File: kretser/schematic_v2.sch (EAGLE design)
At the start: 16 parts, among them IC1 ATMEGA168-20PU, U2 LM2940CT-5.0/NOPB

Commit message: updated krets, updated programs
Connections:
- removed net V_OUT: C2.1, C3.1, C5.1, D2.C, IC1.AVCC, IC1.VCC@1, R2.2, R4.2, SPI.2, U2.OUT
- new net N$2: C3.1, IC1.VCC@1
- new net N$5: C5.1, IC1.AVCC
- new net VCC: C2.1, D2.C, R2.2, R4.2, SPI.2, U2.OUT
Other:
- note added: "LDO_MODULE"
- moved on the sheet: C1, C2, R4, U2

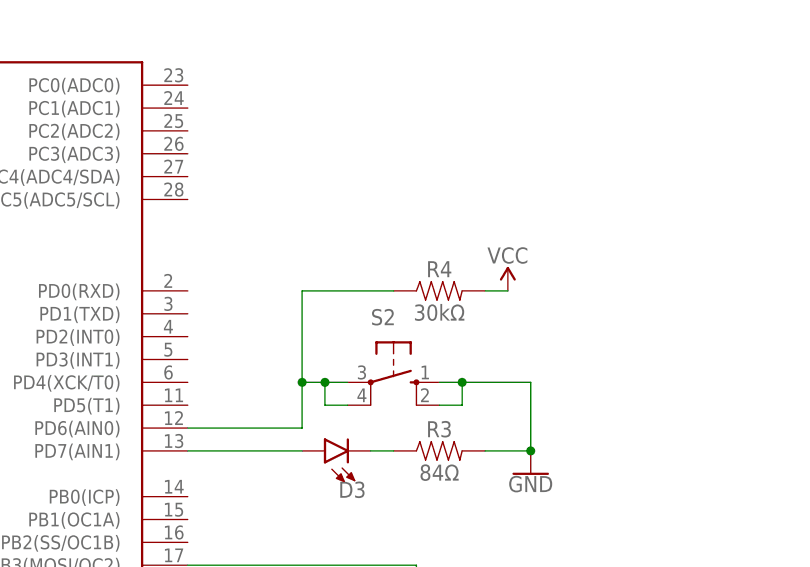
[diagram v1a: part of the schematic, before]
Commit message: updated button codes, updated krets
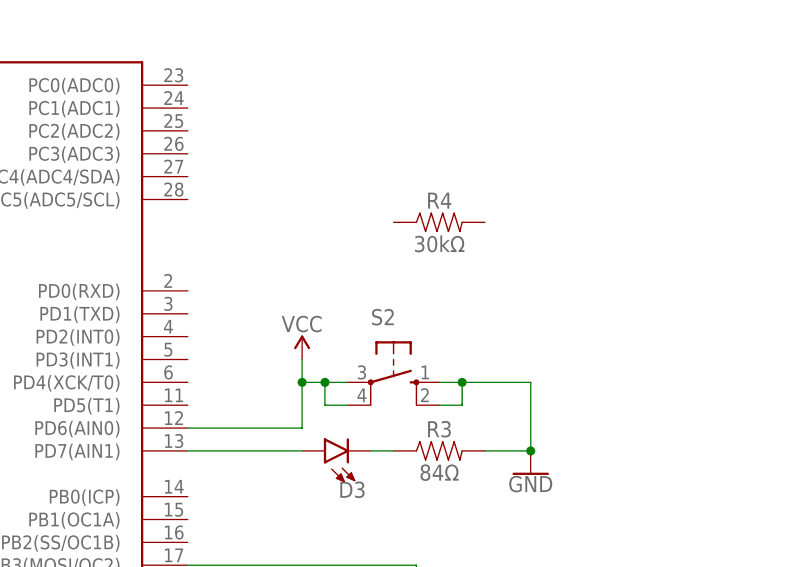
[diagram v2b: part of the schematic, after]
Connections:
- removed net N$8: IC1.PD6(AIN0), R4.1, S2.P, S2.P1
- net VCC: now also IC1.PD6(AIN0), S2.P, S2.P1; no longer R4.2
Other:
- moved on the sheet: R4
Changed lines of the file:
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@@
 <attribute name="VALUE" x="170.815" y="85.09" size="1.778" layer="96"/>
 </instance>
-<instance part="R4" gate="G$1" x="172.72" y="91.44" smashed="yes">
-<attribute name="NAME" x="172.72" y="92.964" size="1.778" layer="95" font="vector" align="bottom-center"/>
-<attribute name="VALUE" x="172.72" y="89.916" size="1.778" layer="96" font="vector" align="top-center"/>
+<instance part="R4" gate="G$1" x="172.72" y="99.06" smashed="yes">
+<attribute name="NAME" x="172.72" y="100.584" size="1.778" layer="95" font="vector" align="bottom-center"/>
+<attribute name="VALUE" x="172.72" y="97.536" size="1.778" layer="96" font="vector" align="top-center"/>
 </instance>
 <instance part="C5" gate="G$1" x="86.36" y="106.68" smashed="yes" rot="R180">
@@
 <attribute name="VALUE" x="73.66" y="139.446" size="1.778" layer="96" font="vector" rot="R180" align="bottom-center"/>
 </instance>
-<instance part="SUPPLY2" gate="G$1" x="180.34" y="91.44" smashed="yes">
-<attribute name="VALUE" x="180.34" y="96.266" size="1.778" layer="96" font="vector" rot="R180" align="bottom-center"/>
+<instance part="SUPPLY2" gate="G$1" x="157.48" y="83.82" smashed="yes">
+<attribute name="VALUE" x="157.48" y="88.646" size="1.778" layer="96" font="vector" rot="R180" align="bottom-center"/>
 </instance>
 <instance part="SUPPLY6" gate="G$1" x="175.26" y="53.34" smashed="yes">
@@
 </segment>
 </net>
-<net name="N$8" class="0">
+<net name="N$1" class="0">
+<segment>
+<pinref part="SPI" gate="G$1" pin="3"/>
+<wire x1="152.4" y1="50.8" x2="147.32" y2="50.8" width="0.1524" layer="91"/>
+<wire x1="147.32" y1="50.8" x2="147.32" y2="55.88" width="0.1524" layer="91"/>
+<pinref part="IC1" gate="G$1" pin="PB5(SCK)"/>
+<wire x1="147.32" y1="55.88" x2="144.78" y2="55.88" width="0.1524" layer="91"/>
+</segment>
+</net>
+<net name="N$3" class="0">
+<segment>
+<pinref part="SPI" gate="G$1" pin="1"/>
+<wire x1="152.4" y1="53.34" x2="149.86" y2="53.34" width="0.1524" layer="91"/>
+<wire x1="149.86" y1="53.34" x2="149.86" y2="58.42" width="0.1524" layer="91"/>
+<pinref part="IC1" gate="G$1" pin="PB4(MISO)"/>
+<wire x1="149.86" y1="58.42" x2="144.78" y2="58.42" width="0.1524" layer="91"/>
+</segment>
+</net>
+<net name="VCC" class="0">
+<segment>
+<wire x1="88.9" y1="134.62" x2="78.74" y2="134.62" width="0.1524" layer="91"/>
+<wire x1="78.74" y1="134.62" x2="73.66" y2="134.62" width="0.1524" layer="91"/>
+<pinref part="D2" gate="1" pin="C"/>
+<wire x1="88.9" y1="124.46" x2="88.9" y2="134.62" width="0.1524" layer="91"/>
+<pinref part="R2" gate="G$1" pin="2"/>
+<wire x1="78.74" y1="129.54" x2="78.74" y2="134.62" width="0.1524" layer="91"/>
+<junction x="78.74" y="134.62"/>
+<pinref part="SUPPLY5" gate="G$1" pin="VCC"/>
+</segment>
+<segment>
+<pinref part="U2" gate="A" pin="OUT"/>
+<wire x1="76.2" y1="170.18" x2="66.04" y2="170.18" width="0.1524" layer="91"/>
+<pinref part="C2" gate="G$1" pin="1"/>
+<wire x1="76.2" y1="165.1" x2="76.2" y2="170.18" width="0.1524" layer="91"/>
+<wire x1="76.2" y1="170.18" x2="81.28" y2="170.18" width="0.1524" layer="91"/>
+<junction x="76.2" y="170.18"/>
+<label x="78.74" y="170.18" size="1.778" layer="95"/>
+</segment>
+<segment>
+<pinref part="SPI" gate="G$1" pin="2"/>
+<wire x1="175.26" y1="53.34" x2="167.64" y2="53.34" width="0.1524" layer="91"/>
+<pinref part="SUPPLY6" gate="G$1" pin="VCC"/>
+</segment>
 <segment>
 <pinref part="S2" gate="1" pin="P"/>
@@
 <wire x1="157.48" y1="81.28" x2="157.48" y2="76.2" width="0.1524" layer="91"/>
 <junction x="160.02" y="81.28"/>
-<pinref part="R4" gate="G$1" pin="1"/>
-<wire x1="167.64" y1="91.44" x2="157.48" y2="91.44" width="0.1524" layer="91"/>
-<wire x1="157.48" y1="91.44" x2="157.48" y2="81.28" width="0.1524" layer="91"/>
+<wire x1="157.48" y1="83.82" x2="157.48" y2="81.28" width="0.1524" layer="91"/>
 <junction x="157.48" y="81.28"/>
-</segment>
-</net>
-<net name="N$1" class="0">
-<segment>
-<pinref part="SPI" gate="G$1" pin="3"/>
-<wire x1="152.4" y1="50.8" x2="147.32" y2="50.8" width="0.1524" layer="91"/>
-<wire x1="147.32" y1="50.8" x2="147.32" y2="55.88" width="0.1524" layer="91"/>
-<pinref part="IC1" gate="G$1" pin="PB5(SCK)"/>
-<wire x1="147.32" y1="55.88" x2="144.78" y2="55.88" width="0.1524" layer="91"/>
-</segment>
-</net>
-<net name="N$3" class="0">
-<segment>
-<pinref part="SPI" gate="G$1" pin="1"/>
-<wire x1="152.4" y1="53.34" x2="149.86" y2="53.34" width="0.1524" layer="91"/>
-<wire x1="149.86" y1="53.34" x2="149.86" y2="58.42" width="0.1524" layer="91"/>
-<pinref part="IC1" gate="G$1" pin="PB4(MISO)"/>
-<wire x1="149.86" y1="58.42" x2="144.78" y2="58.42" width="0.1524" layer="91"/>
-</segment>
-</net>
-<net name="VCC" class="0">
-<segment>
-<wire x1="88.9" y1="134.62" x2="78.74" y2="134.62" width="0.1524" layer="91"/>
-<wire x1="78.74" y1="134.62" x2="73.66" y2="134.62" width="0.1524" layer="91"/>
-<pinref part="D2" gate="1" pin="C"/>
-<wire x1="88.9" y1="124.46" x2="88.9" y2="134.62" width="0.1524" layer="91"/>
-<pinref part="R2" gate="G$1" pin="2"/>
-<wire x1="78.74" y1="129.54" x2="78.74" y2="134.62" width="0.1524" layer="91"/>
-<junction x="78.74" y="134.62"/>
-<pinref part="SUPPLY5" gate="G$1" pin="VCC"/>
-</segment>
-<segment>
-<pinref part="U2" gate="A" pin="OUT"/>
-<wire x1="76.2" y1="170.18" x2="66.04" y2="170.18" width="0.1524" layer="91"/>
-<pinref part="C2" gate="G$1" pin="1"/>
-<wire x1="76.2" y1="165.1" x2="76.2" y2="170.18" width="0.1524" layer="91"/>
-<wire x1="76.2" y1="170.18" x2="81.28" y2="170.18" width="0.1524" layer="91"/>
-<junction x="76.2" y="170.18"/>
-<label x="78.74" y="170.18" size="1.778" layer="95"/>
-</segment>
-<segment>
-<pinref part="R4" gate="G$1" pin="2"/>
-<wire x1="180.34" y1="91.44" x2="177.8" y2="91.44" width="0.1524" layer="91"/>
 <pinref part="SUPPLY2" gate="G$1" pin="VCC"/>
 </segment>
-<segment>
-<pinref part="SPI" gate="G$1" pin="2"/>
-<wire x1="175.26" y1="53.34" x2="167.64" y2="53.34" width="0.1524" layer="91"/>
-<pinref part="SUPPLY6" gate="G$1" pin="VCC"/>
-</segment>
-</net>
+</net>

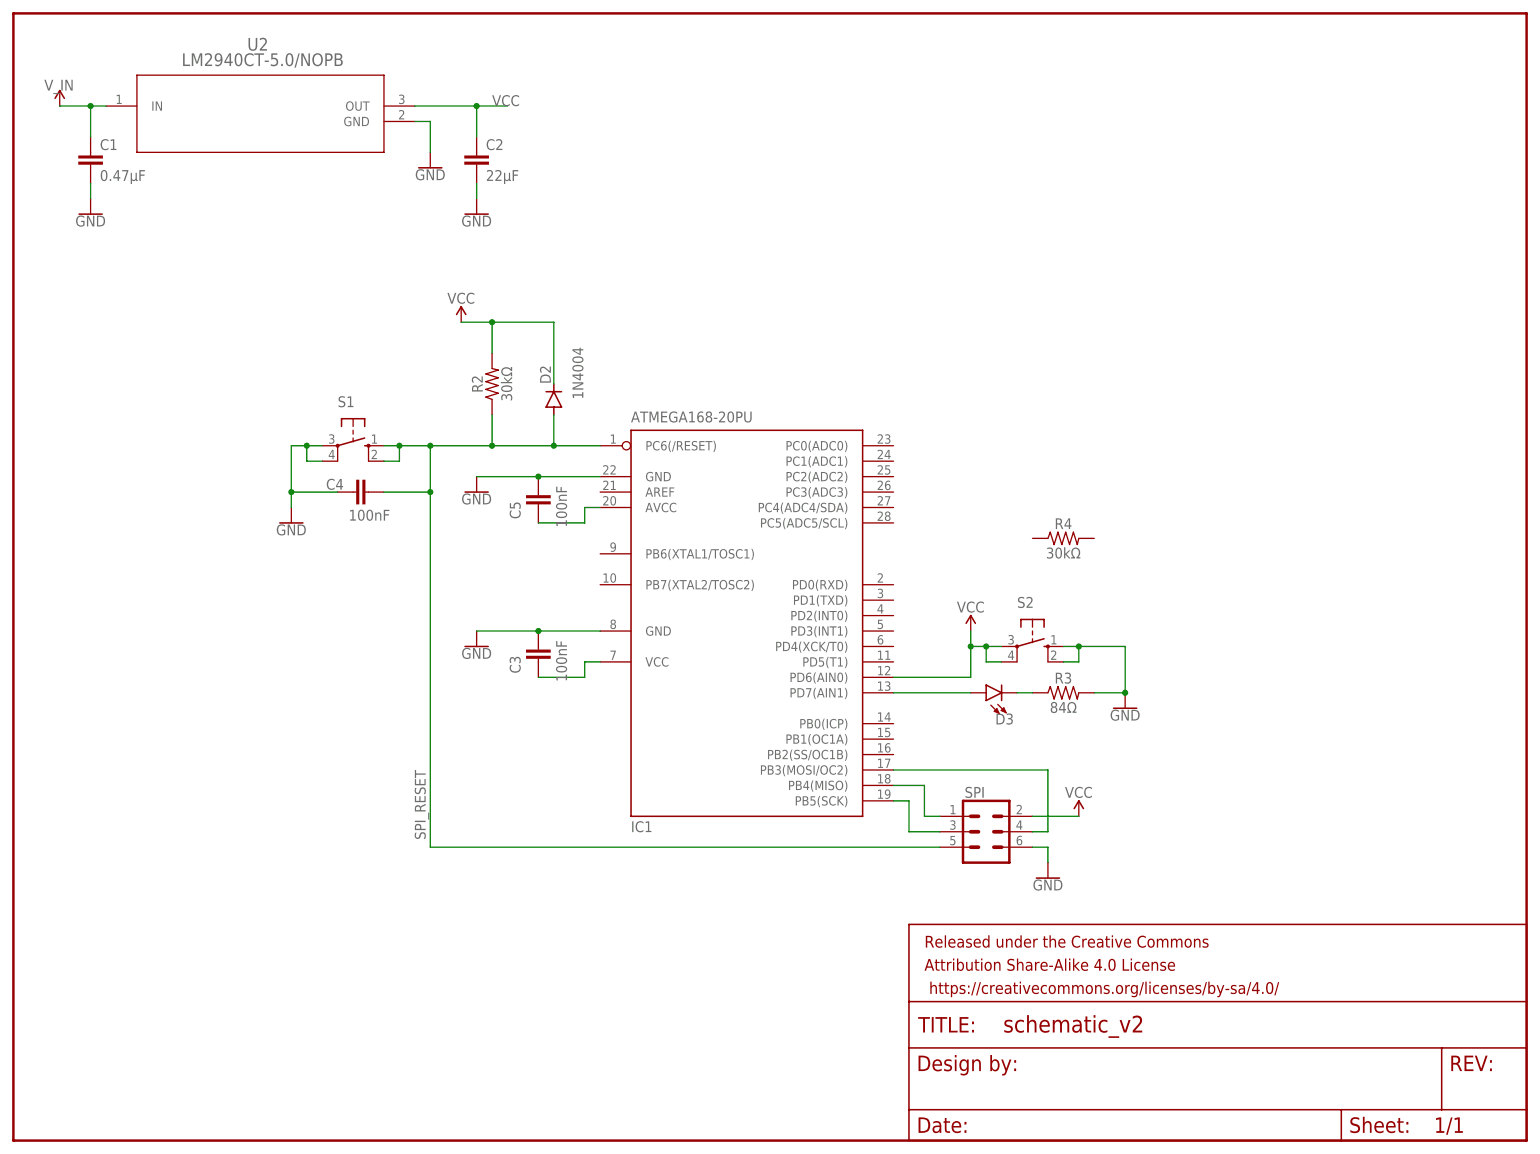
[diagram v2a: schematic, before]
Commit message: Fixed Capacitor parallel connection & resistor value 84 to 330 on main circuit.
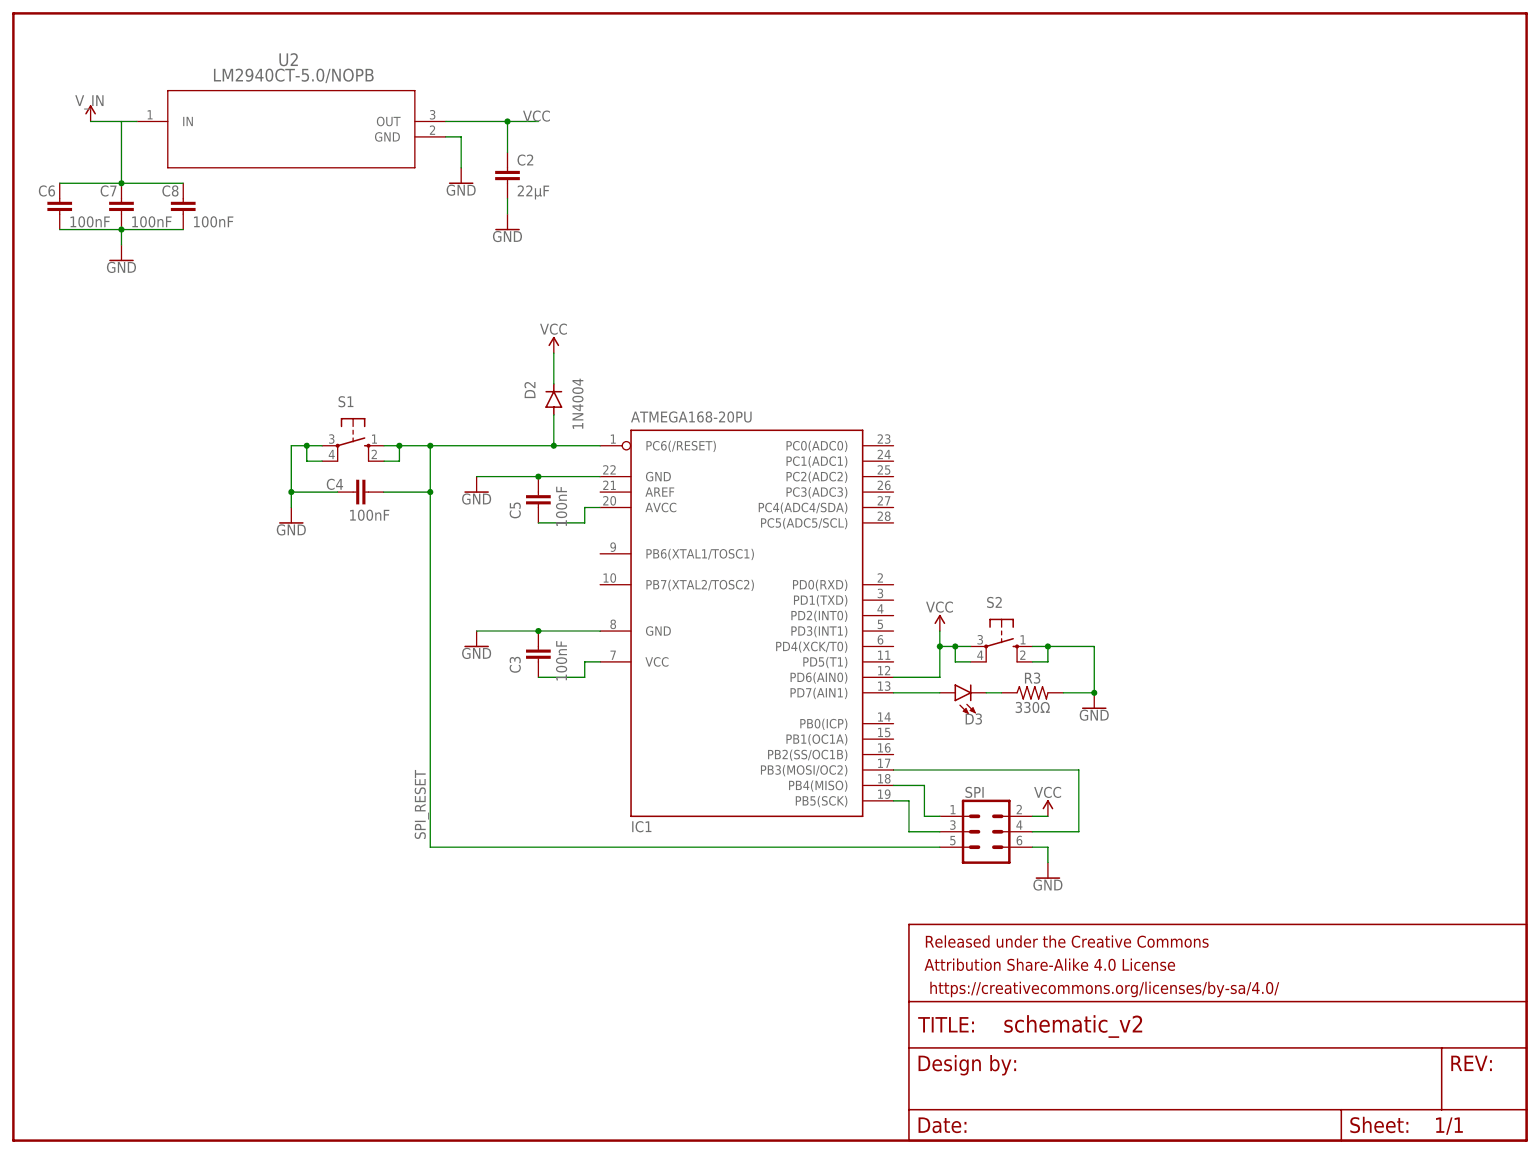
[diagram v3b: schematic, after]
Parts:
- removed C1: 0.47µF, SparkFun-Capacitors:470PF-0603-50V-5%
- removed R2, R4: 30kΩ, SparkFun-Resistors:10OHM-HORIZ-1/4W-1%
- added C6, C7, C8: 100nF, SparkFun-Capacitors:470PF-0603-50V-5%
- R3: value 84Ω -> 330Ω
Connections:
- new net GND1: C6.2, C7.2, C8.2
- new net V_IN1: C6.1, C7.1, C8.1
- net GND: no longer C1.2
- net SPI_RESET: no longer R2.1
- net VCC: no longer R2.2
- net V_IN: no longer C1.1
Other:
- moved on the sheet: C2, D3, R3, S2, U2

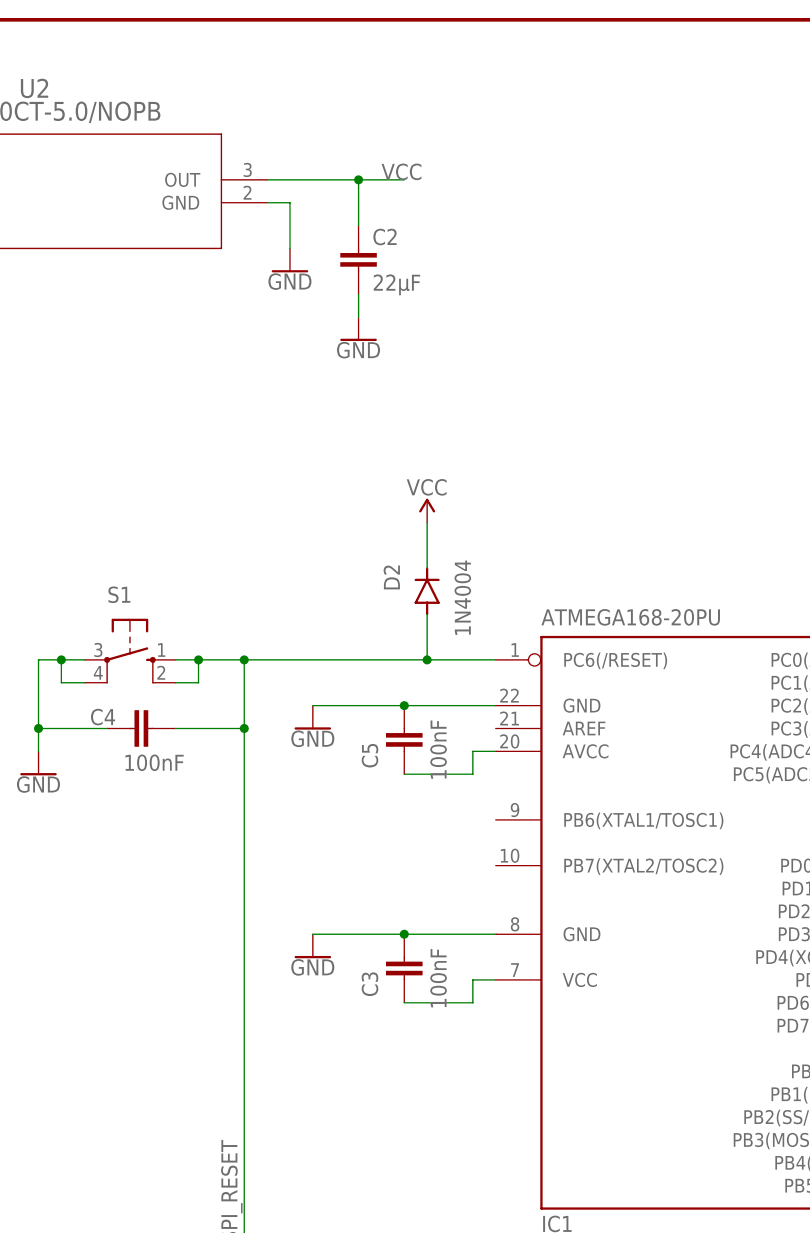
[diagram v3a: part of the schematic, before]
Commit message: Fixed Vcc symbols for MCU Circuit
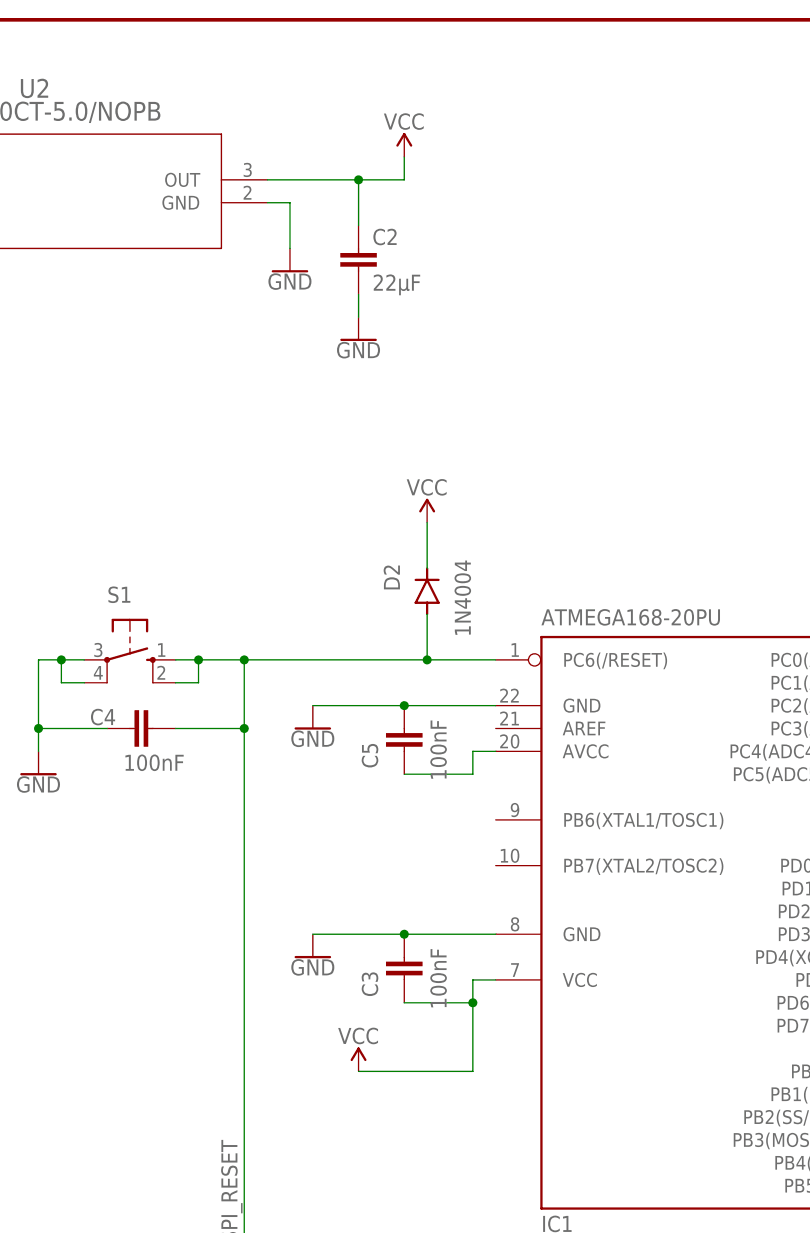
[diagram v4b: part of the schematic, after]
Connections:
- removed net N$2: C3.1, IC1.VCC@1
- net VCC: now also C3.1, IC1.VCC@1
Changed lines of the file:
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@@
 <attribute name="SPICEPREFIX" value="C"/>
 </part>
+<part name="SUPPLY3" library="SparkFun-PowerSymbols" library_urn="urn:adsk.eagle:library:530" deviceset="VCC" device="" value="VCC"/>
+<part name="SUPPLY4" library="SparkFun-PowerSymbols" library_urn="urn:adsk.eagle:library:530" deviceset="VCC" device="" value="VCC"/>
 </parts>
 <sheets>
@@
 <attribute name="NAME" x="24.384" y="155.321" size="1.778" layer="95" font="vector"/>
 <attribute name="VALUE" x="29.464" y="150.241" size="1.778" layer="96" font="vector"/>
+</instance>
+<instance part="SUPPLY3" gate="G$1" x="86.36" y="170.18" smashed="yes">
+<attribute name="VALUE" x="86.36" y="175.006" size="1.778" layer="96" font="vector" rot="R180" align="bottom-center"/>
+</instance>
+<instance part="SUPPLY4" gate="G$1" x="81.28" y="68.58" smashed="yes">
+<attribute name="VALUE" x="81.28" y="73.406" size="1.778" layer="96" font="vector" rot="R180" align="bottom-center"/>
 </instance>
 </instances>
@@
 <wire x1="81.28" y1="167.64" x2="86.36" y2="167.64" width="0.1524" layer="91"/>
 <junction x="81.28" y="167.64"/>
-<label x="83.82" y="167.64" size="1.778" layer="95"/>
+<wire x1="86.36" y1="167.64" x2="86.36" y2="170.18" width="0.1524" layer="91"/>
+<pinref part="SUPPLY3" gate="G$1" pin="VCC"/>
 </segment>
 <segment>
@@
 <pinref part="SUPPLY2" gate="G$1" pin="VCC"/>
 </segment>
-</net>
-<net name="N$2" class="0">
-<segment>
+<segment>
+<pinref part="SUPPLY4" gate="G$1" pin="VCC"/>
 <pinref part="IC1" gate="G$1" pin="VCC@1"/>
 <wire x1="96.52" y1="78.74" x2="93.98" y2="78.74" width="0.1524" layer="91"/>
@@
 <pinref part="C3" gate="G$1" pin="1"/>
 <wire x1="93.98" y1="76.2" x2="86.36" y2="76.2" width="0.1524" layer="91"/>
-</segment>
-</net>
+<wire x1="81.28" y1="68.58" x2="93.98" y2="68.58" width="0.1524" layer="91"/>
+<wire x1="93.98" y1="68.58" x2="93.98" y2="76.2" width="0.1524" layer="91"/>
+<junction x="93.98" y="76.2"/>
+</segment>
+</net>
